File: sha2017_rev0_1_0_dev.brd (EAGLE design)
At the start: 95 x 86 mm, 117 parts, among them IC1 AP7215, IC2 CPT112, IC3 CP210X_USB_UART, IC4 ESP32WROOM32, IC5 MCP73833, IC6 FXL6408, Q1 MMBT2222A, Q2 MMBT2222A, Q3 SI1304 BDL, Q4 MOSFET-PCHANNEL, Q5 MMBT2222A, Q6 MOSFET-PCHANNEL, Q7 MMBT2222A, Q8 MMBT2222A, T1 SI2301DS, X1_ JST-PH3, X701 2908-05WB-MG

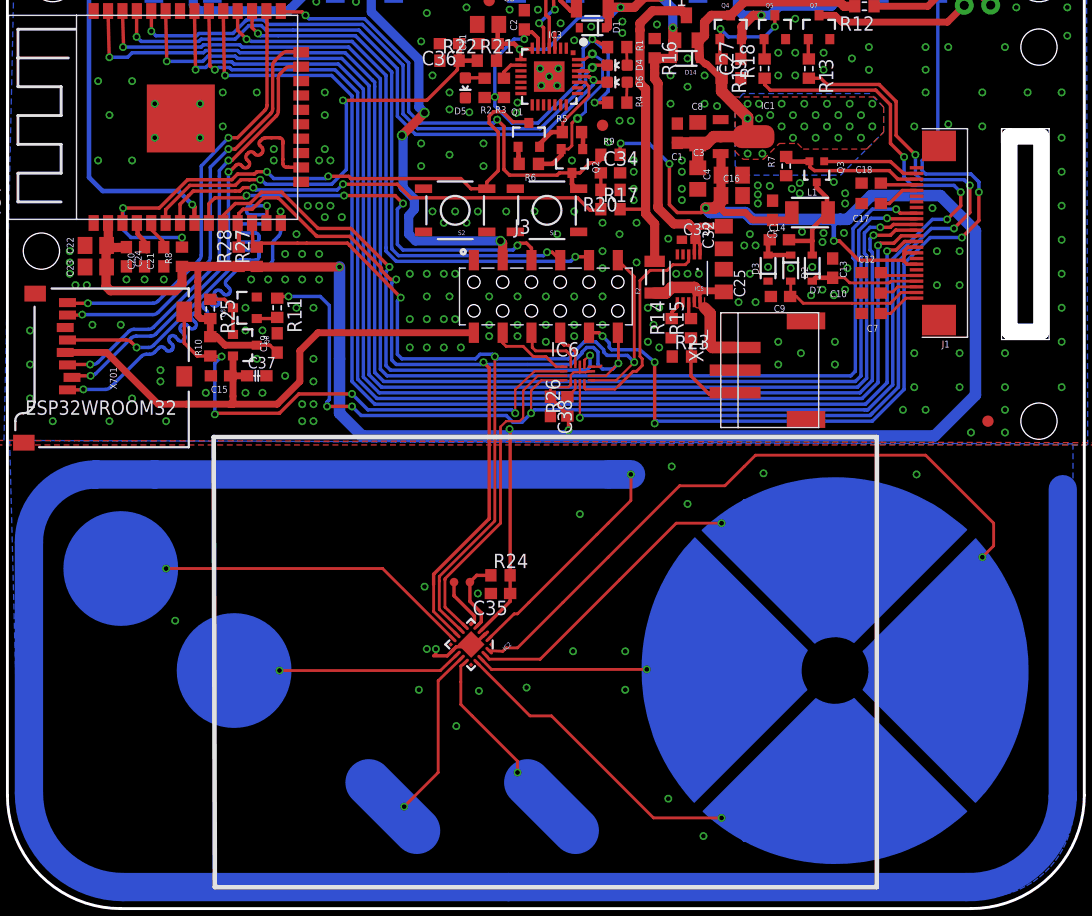
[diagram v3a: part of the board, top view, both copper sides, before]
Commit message: add spezial vias to touch arrea to trick DRC
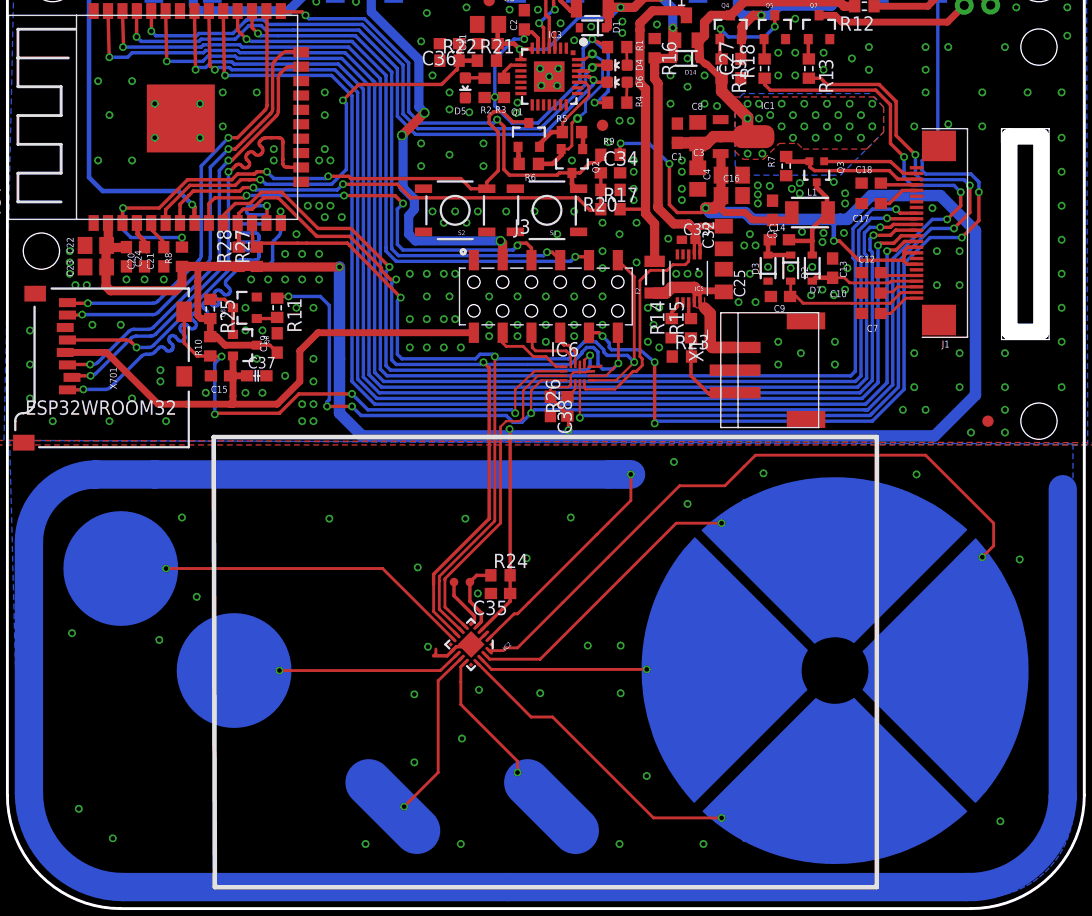
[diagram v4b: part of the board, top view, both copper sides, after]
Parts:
- added U$10, U$11, U$12, U$13, U$14, U$15, U$16, U$17, U$18, U$19, U$2, U$20, U$21, U$22, U$23, U$24, U$25, U$26, U$27, U$28, U$29, U$3, U$30, U$31, U$4, U$5, U$6: VIA, badge:VIA
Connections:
- net GND: now also U$10.P$1, U$11.P$1, U$12.P$1, U$13.P$1, U$14.P$1, U$15.P$1, U$16.P$1, U$17.P$1, U$18.P$1, U$19.P$1, U$2.P$1, U$20.P$1, U$21.P$1, U$22.P$1, U$23.P$1, U$24.P$1, U$25.P$1, U$26.P$1, U$27.P$1, U$28.P$1, U$29.P$1, U$3.P$1, U$30.P$1, U$31.P$1, U$4.P$1, U$5.P$1, U$6.P$1
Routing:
- net GND: vias 297 -> 283
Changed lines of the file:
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@@
 <setting verticaltext="up"/>
 </settings>
-<grid distance="0.1" unitdist="mm" unit="mm" style="lines" multiple="1" display="yes" altdistance="0.025" altunitdist="inch" altunit="inch"/>
+<grid distance="0.01" unitdist="mm" unit="mm" style="lines" multiple="1" display="yes" altdistance="0.025" altunitdist="inch" altunit="inch"/>
 <layers>
 <layer number="1" name="Top" color="4" fill="1" visible="yes" active="yes"/>
@@
 </element>
 <element name="J3" library="EAGLE-BOARD-TO-BOARD_CONNECTORS-rev16c" package="610X12243021" value="" x="47.5" y="53"/>
+<element name="U$2" library="badge" package="VIA" value="VIA" x="6.3" y="7.8"/>
+<element name="U$3" library="badge" package="VIA" value="VIA" x="9.3" y="5.2"/>
+<element name="U$4" library="badge" package="VIA" value="VIA" x="31.6" y="4.7"/>
+<element name="U$5" library="badge" package="VIA" value="VIA" x="40" y="4.7"/>
+<element name="U$6" library="badge" package="VIA" value="VIA" x="54" y="4.7"/>
+<element name="U$10" library="badge" package="VIA" value="VIA" x="61.4" y="4.7"/>
+<element name="U$11" library="badge" package="VIA" value="VIA" x="56.4" y="10.7"/>
+<element name="U$12" library="badge" package="VIA" value="VIA" x="35.9" y="17.9"/>
+<element name="U$13" library="badge" package="VIA" value="VIA" x="40.1" y="14"/>
+<element name="U$14" library="badge" package="VIA" value="VIA" x="47" y="18"/>
+<element name="U$15" library="badge" package="VIA" value="VIA" x="51.2" y="22.2"/>
+<element name="U$16" library="badge" package="VIA" value="VIA" x="54.1" y="22.2"/>
+<element name="U$17" library="badge" package="VIA" value="VIA" x="54.1" y="18"/>
+<element name="U$18" library="badge" package="VIA" value="VIA" x="49.7" y="33.5"/>
+<element name="U$19" library="badge" package="VIA" value="VIA" x="58.8" y="38.4"/>
+<element name="U$20" library="badge" package="VIA" value="VIA" x="87.6" y="6.7"/>
+<element name="U$21" library="badge" package="VIA" value="VIA" x="5.7" y="23.3"/>
+<element name="U$22" library="badge" package="VIA" value="VIA" x="13.4" y="22.7"/>
+<element name="U$23" library="badge" package="VIA" value="VIA" x="16.7" y="26.5"/>
+<element name="U$24" library="badge" package="VIA" value="VIA" x="15.4" y="33.5"/>
+<element name="U$25" library="badge" package="VIA" value="VIA" x="40.4" y="33.4"/>
+<element name="U$26" library="badge" package="VIA" value="VIA" x="36.2" y="29.1"/>
+<element name="U$27" library="badge" package="VIA" value="VIA" x="37.1" y="22.1"/>
+<element name="U$28" library="badge" package="VIA" value="VIA" x="45.8" y="29.9"/>
+<element name="U$29" library="badge" package="VIA" value="VIA" x="28.4" y="33.4"/>
+<element name="U$30" library="badge" package="VIA" value="VIA" x="35.9" y="11.9"/>
+<element name="U$31" library="badge" package="VIA" value="VIA" x="89.3" y="29.8"/>
 </elements>
 <signals>
@@
 <wire x1="39.6" y1="22.1" x2="40.4" y2="22.1" width="0.3048" layer="1"/>
 <wire x1="40.4" y1="22.1" x2="40.9" y2="22.6" width="0.3048" layer="1"/>
-<wire x1="40.9" y1="22.6" x2="41.5" y2="22.6" width="0.3048" layer="1"/>
-<wire x1="41.5" y1="22.6" x2="42.1" y2="23.2" width="0.3048" layer="1"/>
-<wire x1="42.1" y1="23.2" x2="42.156303125" y2="23.1991625" width="0.3048" layer="1"/>
+<wire x1="40.9" y1="22.6" x2="41.52" y2="22.59" width="0.3048" layer="1"/>
 <wire x1="39.2925625" y1="21.78195625" x2="38.8" y2="21.3" width="0.3048" layer="1"/>
 <wire x1="38.8" y1="21.3" x2="37.6" y2="21.3" width="0.3048" layer="1"/>
 <via x="41.5" y="26.8" extent="1-16" drill="0.4"/>
-<via x="37.8" y="21.9" extent="1-16" drill="0.4"/>
-<via x="37" y="21.9" extent="1-16" drill="0.4"/>
 <wire x1="37.6" y1="21.3" x2="37.8" y2="21.5" width="0.254" layer="1"/>
 <wire x1="37.8" y1="21.5" x2="37.8" y2="21.9" width="0.254" layer="1"/>
-<via x="49.9" y="21.7" extent="1-16" drill="0.4"/>
-<via x="45.8" y="18.5" extent="1-16" drill="0.4"/>
-<via x="41.6" y="18.2" extent="1-16" drill="0.4"/>
-<via x="39.6" y="15.1" extent="1-16" drill="0.4"/>
-<via x="36.3" y="18.3" extent="1-16" drill="0.4"/>
-<via x="36.8" y="27.4" extent="1-16" drill="0.4"/>
 <via x="60" y="34.7" extent="1-16" drill="0.4"/>
-<via x="58.6" y="38" extent="1-16" drill="0.4"/>
-<via x="50.5" y="33.8" extent="1-16" drill="0.4"/>
 <via x="80.2" y="37.3" extent="1-16" drill="0.4"/>
 <via x="66.7" y="37.4" extent="1-16" drill="0.4"/>
-<via x="54.5" y="21.7" extent="1-16" drill="0.4"/>
-<via x="54.5" y="18.3" extent="1-16" drill="0.4"/>
-<via x="58.3" y="8.7" extent="1-16" drill="0.4"/>
-<via x="61.4" y="5.4" extent="1-16" drill="0.4"/>
-<via x="14.8" y="24.4" extent="1-16" drill="0.4"/>
 <contactref element="Q8" pad="2"/>
 <contactref element="C37" pad="2"/>
@@
 <via x="26" y="42" extent="1-16" drill="0.4"/>
 <via x="27" y="42" extent="1-16" drill="0.4"/>
+<contactref element="U$15" pad="P$1"/>
+<contactref element="U$16" pad="P$1"/>
+<contactref element="U$17" pad="P$1"/>
+<contactref element="U$18" pad="P$1"/>
+<contactref element="U$19" pad="P$1"/>
+<contactref element="U$20" pad="P$1"/>
+<contactref element="U$11" pad="P$1"/>
+<contactref element="U$12" pad="P$1"/>
+<contactref element="U$13" pad="P$1"/>
+<contactref element="U$14" pad="P$1"/>
+<contactref element="U$2" pad="P$1"/>
+<contactref element="U$10" pad="P$1"/>
+<contactref element="U$6" pad="P$1"/>
+<contactref element="U$5" pad="P$1"/>
+<contactref element="U$4" pad="P$1"/>
+<contactref element="U$3" pad="P$1"/>
+<contactref element="U$21" pad="P$1"/>
+<contactref element="U$22" pad="P$1"/>
+<contactref element="U$23" pad="P$1"/>
+<contactref element="U$24" pad="P$1"/>
+<contactref element="U$25" pad="P$1"/>
+<contactref element="U$26" pad="P$1"/>
+<contactref element="U$27" pad="P$1"/>
+<contactref element="U$28" pad="P$1"/>
+<contactref element="U$29" pad="P$1"/>
+<contactref element="U$30" pad="P$1"/>
+<contactref element="U$31" pad="P$1"/>
+<via x="41.6" y="18.3" extent="1-16" drill="0.4"/>
+<wire x1="42.156303125" y1="23.1991625" x2="41.52" y2="22.59" width="0.254" layer="1"/>
 </signal>
 <signal name="USB_DN_CON">
@@
 <wire x1="29.9" y1="70" x2="29.6" y2="70.3" width="0.3048" layer="16"/>
 <via x="29.6" y="70.3" extent="1-16" drill="0.4"/>
-<wire x1="29.6" y1="70.3" x2="37" y2="70.3" width="0.3048" layer="1"/>
-<wire x1="37" y1="70.3" x2="39.7" y2="73" width="0.3048" layer="1"/>
 <wire x1="39.7" y1="73" x2="39.7" y2="73.65" width="0.3048" layer="1"/>
 <wire x1="39.7" y1="73.65" x2="39.85" y2="73.8" width="0.3048" layer="1"/>
+<wire x1="29.6" y1="70.3" x2="31" y2="71.7" width="0.3048" layer="1"/>
+<wire x1="31" y1="71.7" x2="38.3" y2="71.7" width="0.3048" layer="1"/>
+<wire x1="38.3" y1="71.7" x2="39.6" y2="73" width="0.3048" layer="1"/>
+<wire x1="39.6" y1="73" x2="39.7" y2="73" width="0.3048" layer="1"/>
 </signal>
 <signal name="WS2812_DATA">
@@
 <contactref element="IC2" pad="19"/>
 <contactref element="TB5" pad="UP"/>
-<wire x1="42.14849375" y1="21.401465625" x2="42.5" y2="21" width="0.254" layer="1"/>
-<wire x1="42.5" y1="21" x2="47" y2="21" width="0.254" layer="1"/>
+<wire x1="42.14849375" y1="21.401465625" x2="42.54" y2="21" width="0.254" layer="1"/>
+<wire x1="42.54" y1="21" x2="47" y2="21" width="0.254" layer="1"/>
 <wire x1="47" y1="21" x2="54" y2="28" width="0.254" layer="1"/>
 <wire x1="54" y1="28" x2="59" y2="33" width="0.254" layer="1"/>
@@
 <contactref element="IC2" pad="17"/>
 <contactref element="TB5" pad="D"/>
-<wire x1="41.437796875" y1="20.690765625" x2="46.1" y2="16" width="0.254" layer="1"/>
-<wire x1="46.1" y1="16" x2="48" y2="16" width="0.254" layer="1"/>
-<wire x1="48" y1="16" x2="57" y2="7" width="0.254" layer="1"/>
+<wire x1="41.437796875" y1="20.690765625" x2="46.2" y2="15.9" width="0.254" layer="1"/>
+<wire x1="46.2" y1="15.9" x2="48.1" y2="15.9" width="0.254" layer="1"/>
+<wire x1="48.1" y1="15.9" x2="57" y2="7" width="0.254" layer="1"/>
 <wire x1="57" y1="7" x2="63" y2="7" width="0.254" layer="1"/>
 <via x="63" y="7" extent="1-16" drill="0.4"/>
@@
 <contactref element="TB4" pad="P$1"/>
 <contactref element="IC2" pad="15"/>
-<wire x1="40.376571875" y1="20.708725" x2="40" y2="20.4" width="0.254" layer="1"/>
-<wire x1="40" y1="20.4" x2="40" y2="19" width="0.254" layer="1"/>
+<wire x1="40.376571875" y1="20.708725" x2="40" y2="20.33" width="0.254" layer="1"/>
+<wire x1="40" y1="20.33" x2="40" y2="19" width="0.254" layer="1"/>
 <wire x1="40" y1="19" x2="40" y2="17" width="0.254" layer="1"/>
 <wire x1="40" y1="17" x2="41" y2="16" width="0.254" layer="1"/>
@@
 <contactref element="IC2" pad="20"/>
 <contactref element="TB5" pad="L"/>
-<wire x1="42.49845625" y1="21.751421875" x2="43.7" y2="21.7" width="0.254" layer="1"/>
-<wire x1="43.7" y1="21.7" x2="44" y2="22" width="0.254" layer="1"/>
+<wire x1="42.49845625" y1="21.751421875" x2="43.74" y2="21.76" width="0.254" layer="1"/>
+<wire x1="43.74" y1="21.76" x2="44" y2="22" width="0.254" layer="1"/>
 <wire x1="44" y1="22" x2="45" y2="22" width="0.254" layer="1"/>
 <wire x1="45" y1="22" x2="49" y2="26" width="0.254" layer="1"/>

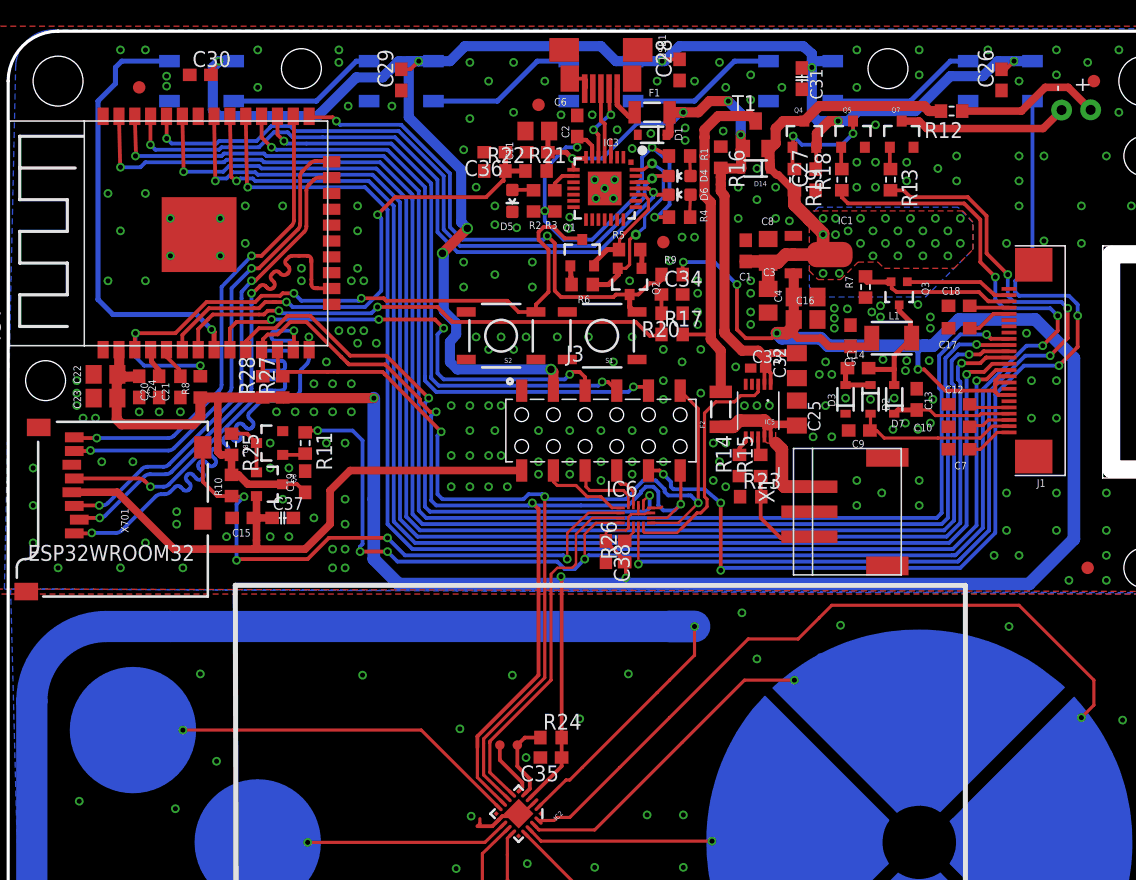
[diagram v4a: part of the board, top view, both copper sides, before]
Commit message: added most of the test points
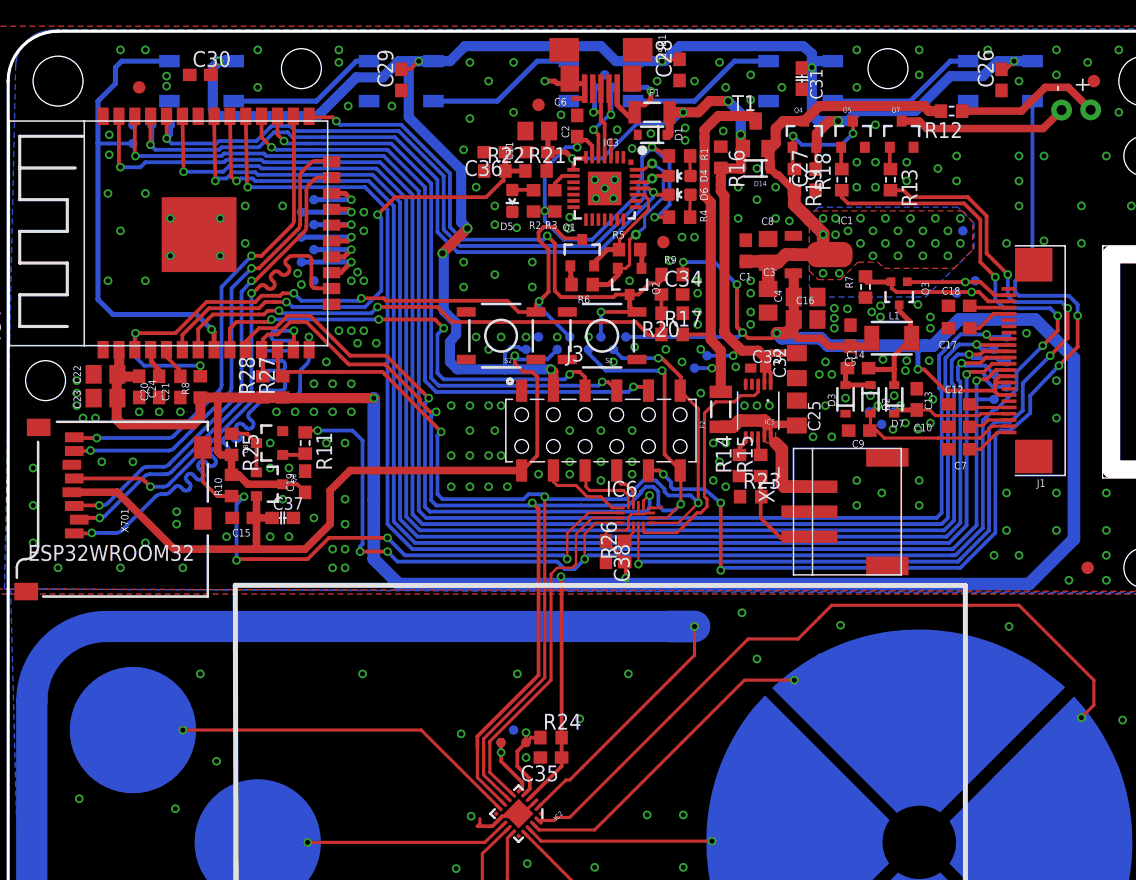
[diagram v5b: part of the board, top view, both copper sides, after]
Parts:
- added TP10, TP11, TP12, TP13, TP14, TP15, TP16, TP17, TP18, TP19, TP20, TP22, TP23, TP24, TP25, TP26, TP27, TP28, TP29, TP3, TP30, TP31, TP32, TP33, TP34, TP35, TP36, TP37, TP38, TP39, TP4, TP40, TP41, TP42, TP43, TP5, TP6, TP7, TP8, TP9: TEST-POINT3, SparkFun-Passives:PAD.03X.03
- moved TP1 0.73 mm to (41.5, 28.0)
- moved U$26 0.41 mm to (36.3, 28.7)
- moved U$25 0.41 mm to (40.8, 33.5)
- moved TP2 0.22 mm to (39.5, 28.0)
- moved U$21 0.20 mm to (5.70, 23.5)
- moved U$29 0.10 mm to (28.4, 33.5)
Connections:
- removed net ESP32_FLASH/TOUCHE_MENU: IC4.25, Q2.3, R9.1, S1.3
- new net ESP32_FLASH: IC4.25, Q2.3, R9.1, S1.3, TP23.P$1
- net +3V3: now also TP28.P$1
- net +5V: now also TP30.P$1
- net 3V3_SWITCHED: now also TP26.P$1
- net ESP32_!RESET: now also TP24.P$1
- net ESP32_RX: now also TP33.P$1
- net ESP32_TX: now also TP34.P$1
- net GDR: now also TP5.P$1
- net GND: now also TP32.P$1, TP38.P$1, TP39.P$1, TP40.P$1, TP41.P$1, TP42.P$1
- net I2C_SCL: now also TP20.P$1
- net I2C_SDA: now also TP22.P$1
- net LCD_!RESET: now also TP8.P$1
- net LCD_BUSY: now also TP7.P$1
- net LCD_CS: now also TP37.P$1
- net LCD_D/!S: now also TP9.P$1
- net LCD_MOSI: now also TP11.P$1
- net LCD_SCK: now also TP10.P$1
- net N$12: now also TP14.P$1
- net N$3: now also TP19.P$1
- net N$32: now also TP43.P$1
- net N$4: now also TP18.P$1
- net N$6: now also TP17.P$1
- net N$61: now also TP3.P$1
- net N$62: now also TP4.P$1
- net N$7: now also TP16.P$1
- net N$9: now also TP15.P$1
- net PREVGH: now also TP12.P$1
- net PREVGL: now also TP13.P$1
- net RESE: now also TP6.P$1
- net USB_DN_CON: now also TP35.P$1
- net USB_DP_CON: now also TP36.P$1
- net VBAT: now also TP27.P$1
- net VCC: now also TP29.P$1
- net WS2812_DATA: now also TP31.P$1
- net WS2812_POWER: now also TP25.P$1
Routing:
- net ESP32_FLASH: track 0.00 -> 47.4 mm, vias 0 -> 3
- net ESP32_FLASH/TOUCHE_MENU: track 42.5 -> 0.00 mm, vias 2 -> 0
- net I2C_SDA: track 88.2 -> 104.0 mm, vias 3 -> 4
- net 3V3_SWITCHED: track 48.7 -> 63.4 mm, vias 0 -> 1
- net +3V3: track 228.0 -> 238.6 mm, vias 7 -> 8
- net I2C_SCL: track 86.5 -> 93.9 mm, vias 3 -> 4
- net N$3: track 0.00 -> 5.93 mm, vias 0 -> 1
- net N$6: track 0.00 -> 5.71 mm, vias 0 -> 1
- net N$9: track 0.00 -> 5.68 mm, vias 0 -> 1
- net N$4: track 0.00 -> 4.82 mm, vias 0 -> 1
- net N$12: track 0.00 -> 4.79 mm, vias 0 -> 1
- net N$7: track 0.00 -> 4.60 mm, vias 0 -> 1
- net ESP32_!RESET: track 55.1 -> 59.4 mm, vias 4 -> 5
- net N$32: track 3.16 -> 7.40 mm, vias 0 -> 1
- net LCD_SCK: track 107.3 -> 111.3 mm
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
